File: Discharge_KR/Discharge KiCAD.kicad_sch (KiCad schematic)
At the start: 13 parts, among them IC1 AL5890-10D-13, J105 Conn_01x02, J3 Conn_01x02, J4 Conn_01x03, J90 Conn_01x02, K1 DBR71210, Q1 2N7000, U2 HCPL-817-000E

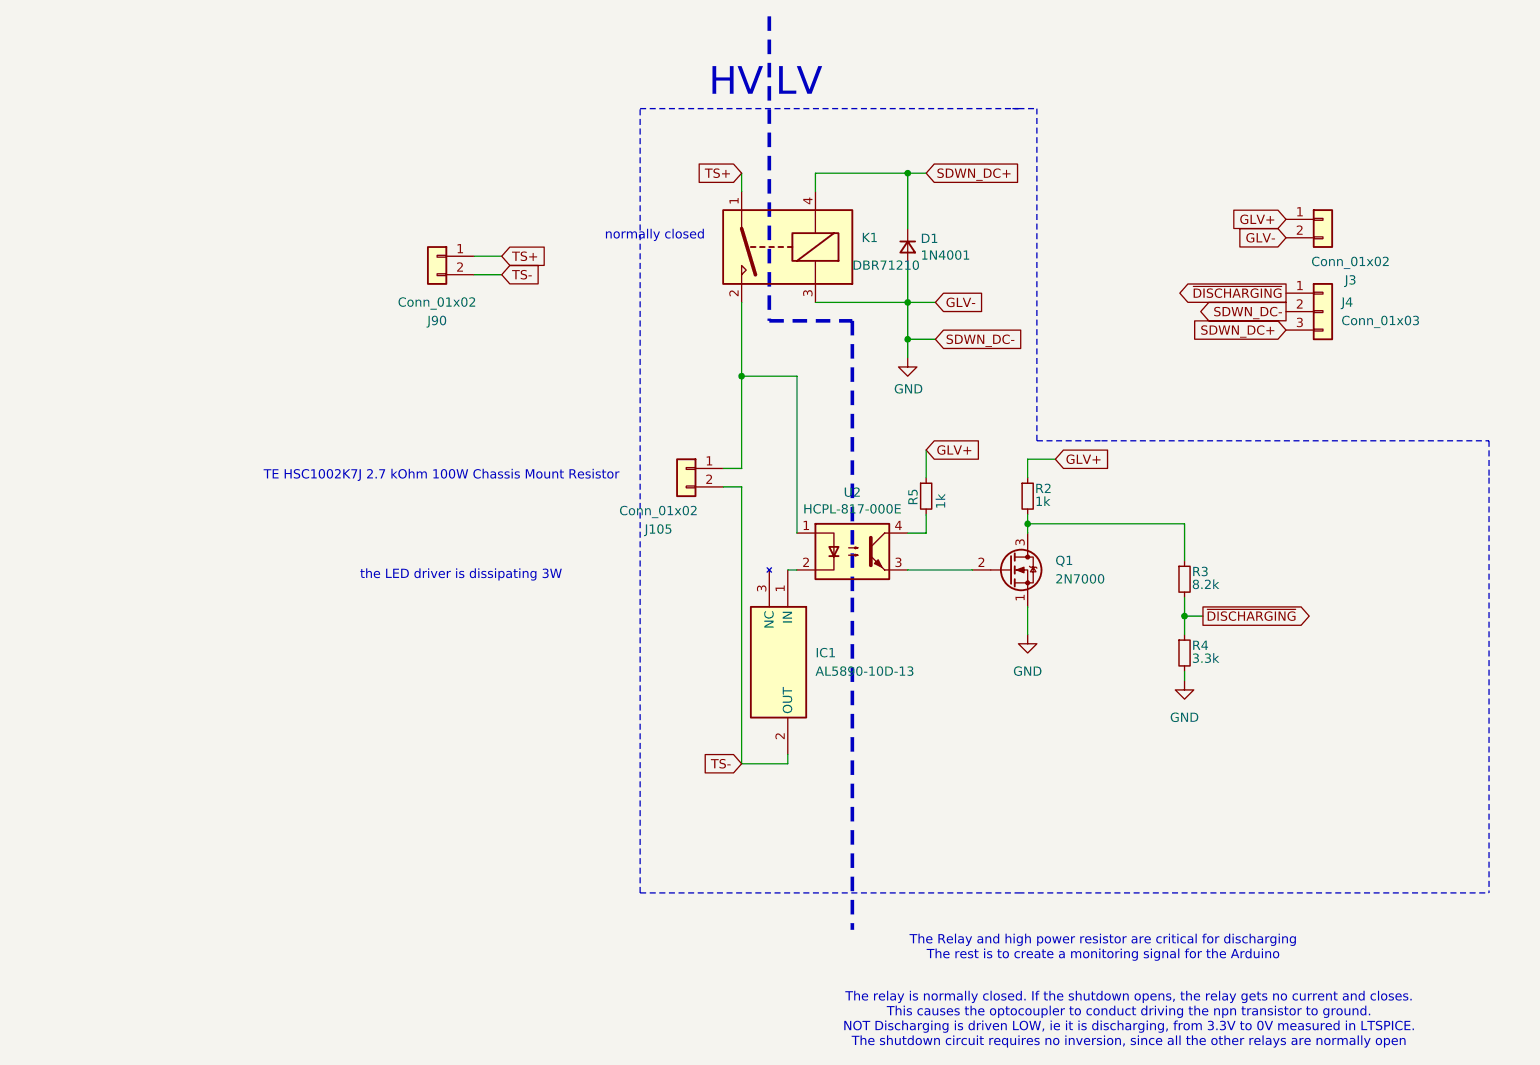
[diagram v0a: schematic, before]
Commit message: precharge and discharge fixed
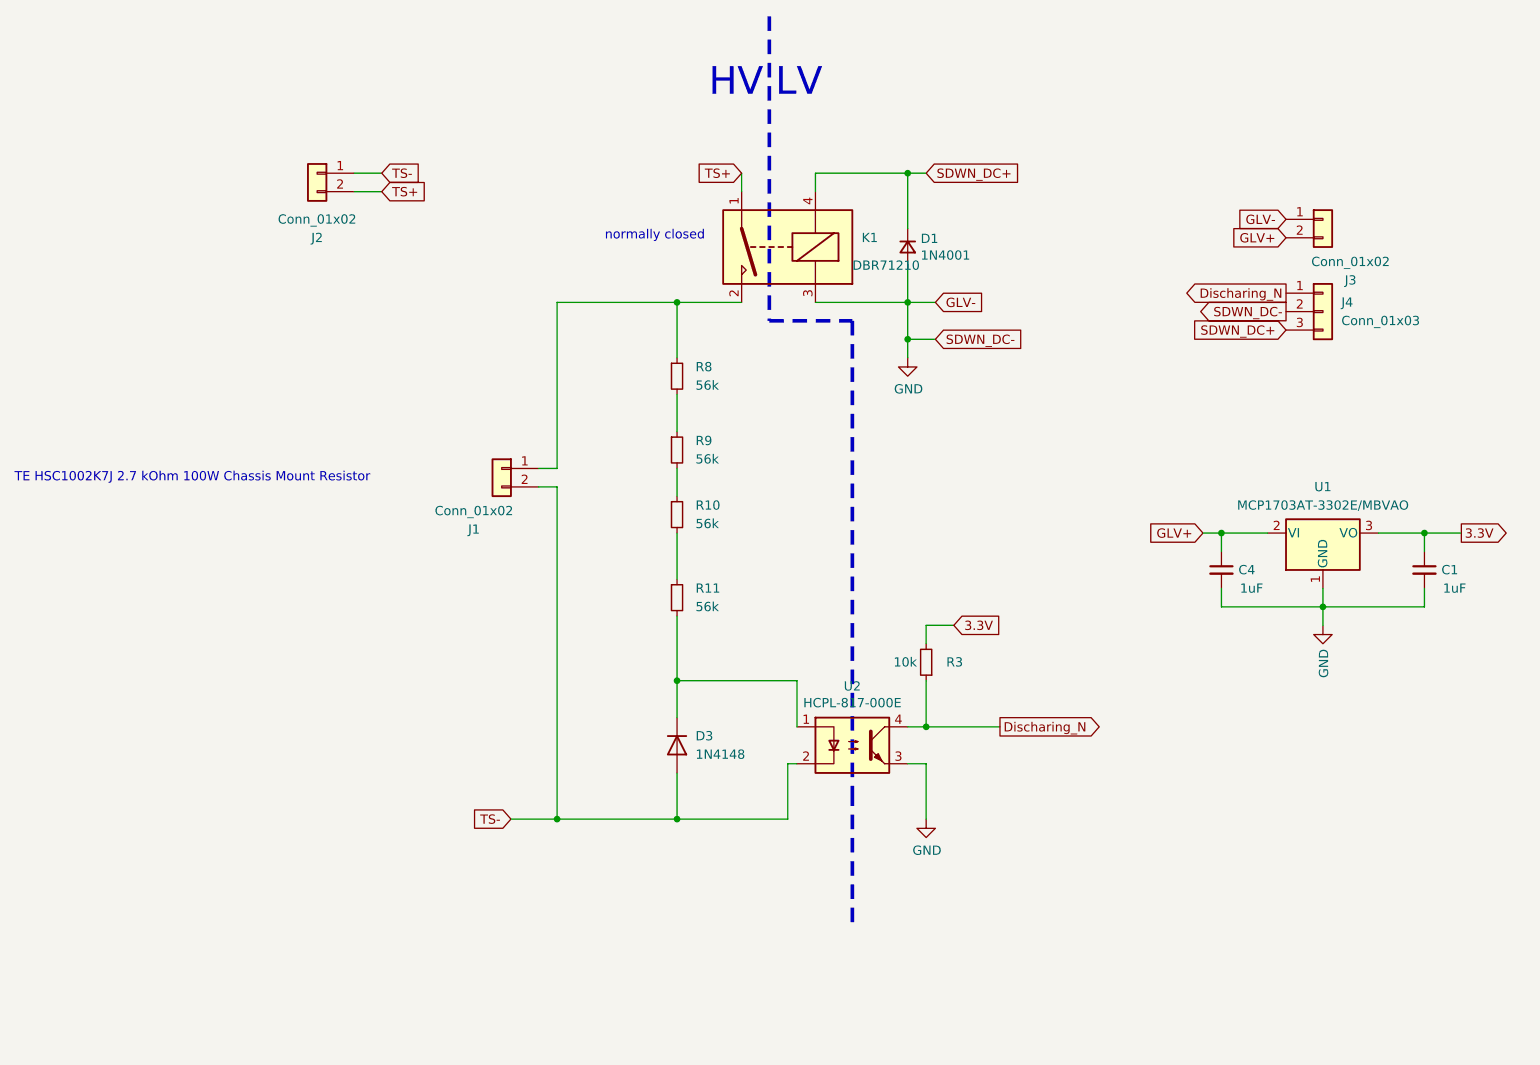
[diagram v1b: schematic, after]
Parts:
- removed IC1: AL5890-10D-13, AL5890_10_D13:AL589010D13, symbol AL5890-10D-13:AL5890-10D-13
- removed Q1: 2N7000, Package_TO_SOT_THT:TO-92_Inline, symbol Transistor_FET:2N7000
- removed R2, R5: 1k, Resistor_THT:R_Axial_DIN0207_L6.3mm_D2.5mm_P10.16mm_Horizontal, symbol Device:R_Small
- removed R4: 3.3k, Resistor_THT:R_Axial_DIN0207_L6.3mm_D2.5mm_P10.16mm_Horizontal, symbol Device:R_Small
- added C1, C4: 1uF, FA14_Capacitor:FA18X7R1H104KNU00, symbol tsal-rescue:C_Small-Device
- added D3: 1N4148, Diode_THT:D_DO-35_SOD27_P7.62mm_Horizontal, symbol Diode:1N4148
- added R10, R11, R8, R9: 56k, Resistor_THT:R_Axial_DIN0207_L6.3mm_D2.5mm_P10.16mm_Horizontal, symbol Device:R_Small
- added U1: MCP1703AT-3302E/MBVAO, Package_TO_SOT_SMD:SOT-89-3, symbol Regulator_Linear:MCP1703Ax-300xxMB
- J3: footprint Phoenix 1x2 Connector:Phoenix_1x2_1729128 -> Connector_JST:JST_XH_B2B-XH-A_1x02_P2.50mm_Vertical; Part Number 1729128 -> B2B-XH-A
- R3: value 8.2k -> 10k; Part Number MCF 0.25W 8K2 -> MCF 0.25W 10K
- renumbered J105 to J1, J90 to J2
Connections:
- net GLV+: now also J3.2 (Pin_2), C4.1, U1.2 (VI); no longer J3.1 (Pin_1)
- net GND: now also J3.1 (Pin_1), U2.3, C1.2, C4.2, U1.1 (GND); no longer J3.2 (Pin_2)
- net TS+: now also J2.2 (Pin_2); no longer J2.1 (Pin_1)
- net TS-: now also J2.1 (Pin_1), U2.2, D3.2 (A); no longer J2.2 (Pin_2)
- net at J1.1 (Pin_1), K1.2: now also R8.1; no longer U2.1
- net Discharing_N: now reaches U2.4
- net Discharing_N: now also J4.1 (Pin_1), R3.1
- net ~{DISCHARGING} renamed 3.3V
- net 3.3V: now also C1.1, U1.3 (VO); no longer J4.1 (Pin_1)
- new net: R8.2, R9.1
- new net: R10.1, R9.2
- new net: D3.1 (K), R11.2, U2.1
- new net: R10.2, R11.1
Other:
- note removed: "The Relay and high power resistor are critical for discharging The rest is to create a monitoring signal for the Arduino"
- note removed: "The relay is normally closed. If the shutdown opens, the relay gets no current and closes. This causes the optocoupler to conduct driving the npn transistor to ground. NOT Discharging is driven LOW, ie it is discharging, from 3.3V to 0V measured in LTSPICE. The shutdown circuit requires no inversion, since all the other relays are normally open"
- note removed: "the LED driver is dissipating 3W"
- moved on the sheet: J1, J2, U2

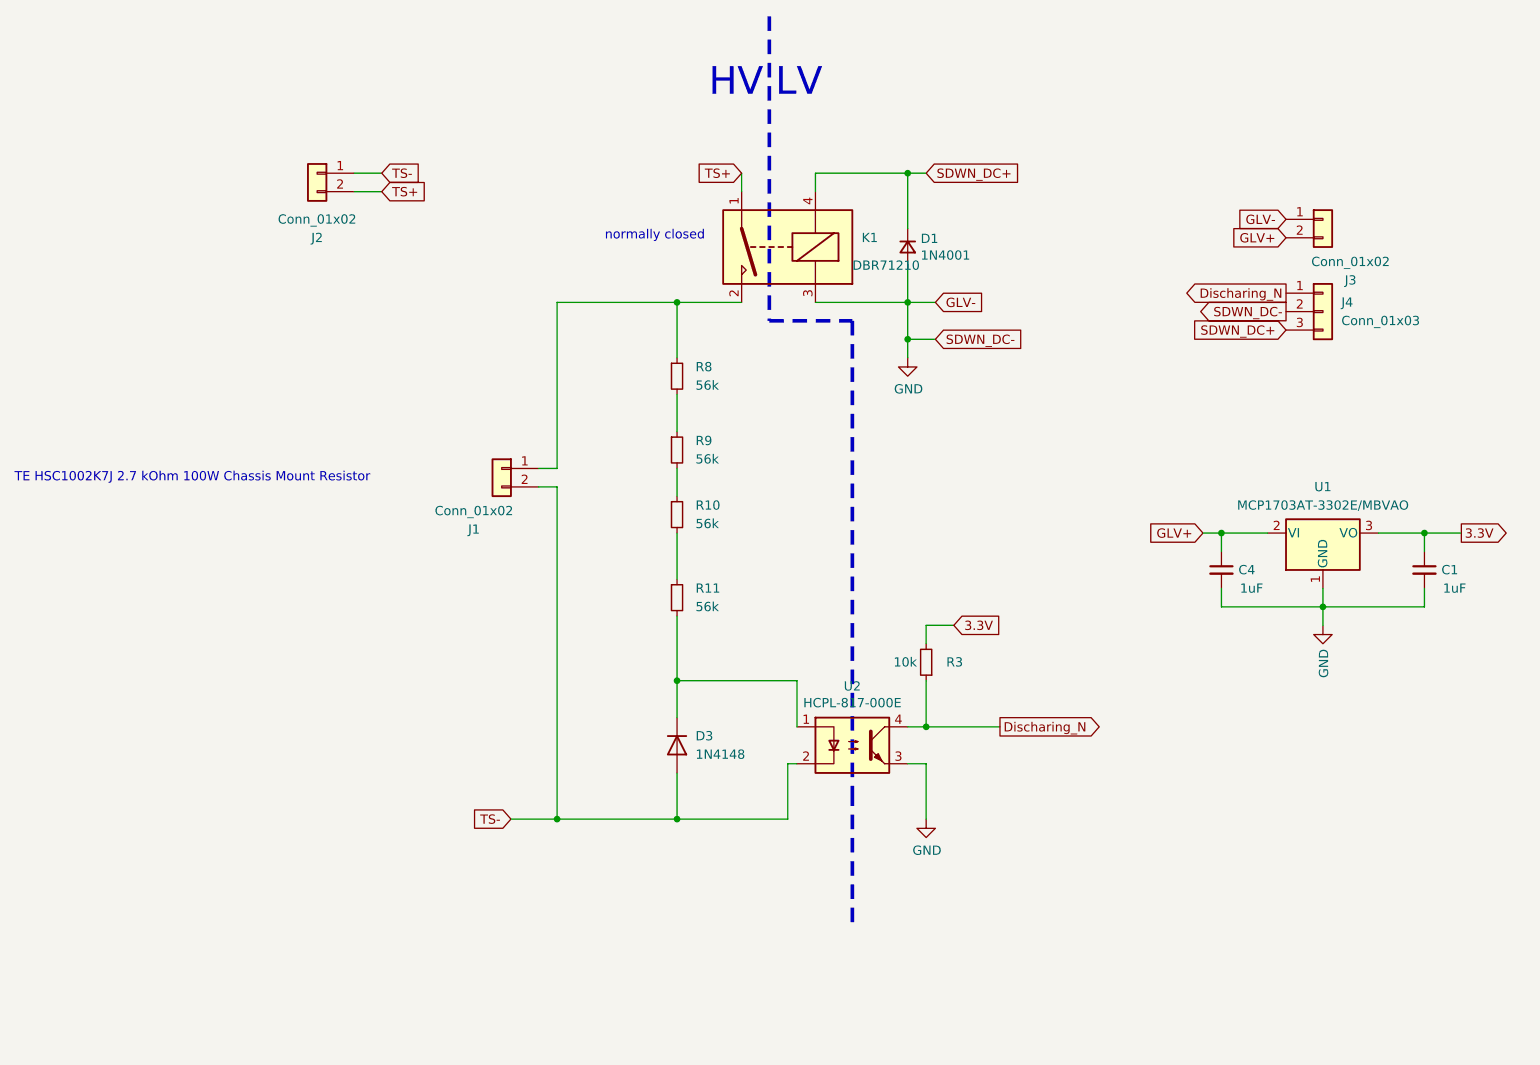
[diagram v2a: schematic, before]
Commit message: Slave with SMD and no other fuses
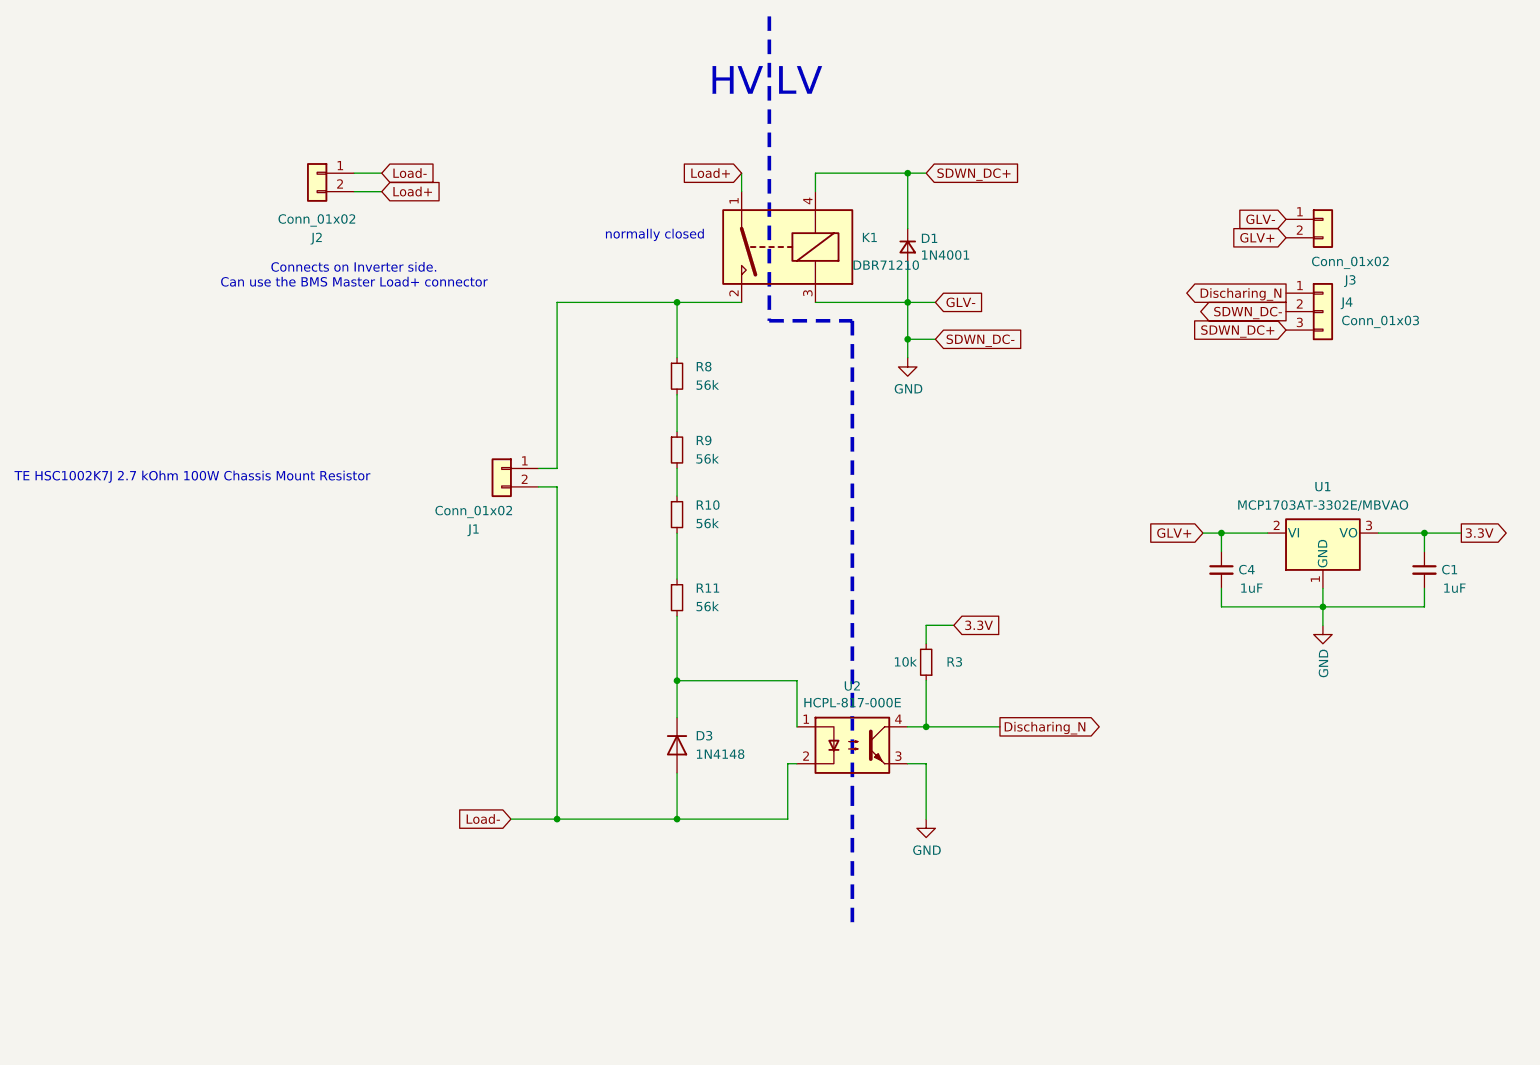
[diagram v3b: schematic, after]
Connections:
- net TS+ renamed Load+
- net TS- renamed Load-
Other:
- note added: "Connects on Inverter side. Can use the BMS Master Load+ connector"
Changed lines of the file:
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@@
+		)
+	)
+	(text "Connects on Inverter side.\nCan use the BMS Master Load+ connector"
+		(exclude_from_sim no)
+		(at 40.64 45.974 0)
+		(effects
+			(font
+				(size 1.27 1.27)
+			)
 		)
 	)
@@
 		)
 	)
-	(global_label "TS+"
+	(global_label "Load+"
 		(shape input)
 		(at 44.45 34.29 0)
@@
 		)
 		(property "Intersheetrefs" "${INTERSHEET_REFS}"
-			(at 50.5305 34.29 0)
+			(at 52.8285 34.29 0)
 			(effects
 				(font
@@
 		)
 	)
-	(global_label "TS-"
+	(global_label "Load-"
 		(shape input)
 		(at 62.23 120.65 180)
@@
 		)
 		(property "Intersheetrefs" "${INTERSHEET_REFS}"
-			(at 56.1495 120.65 0)
+			(at 53.8515 120.65 0)
 			(effects
 				(font
@@
 		)
 	)
-	(global_label "TS-"
+	(global_label "Load-"
 		(shape input)
 		(at 44.45 31.75 0)
@@
 		)
 		(property "Intersheetrefs" "${INTERSHEET_REFS}"
-			(at 50.5305 31.75 0)
+			(at 52.8285 31.75 0)
 			(effects
 				(font
@@
 		)
 	)
-	(global_label "TS+"
+	(global_label "Load+"
 		(shape input)
 		(at 93.98 31.75 180)
@@
 		)
 		(property "Intersheetrefs" "${INTERSHEET_REFS}"
-			(at 87.8995 31.75 0)
-			(effects
-				(font
+			(at 85.6015 31.75 0)
+			(effects
+				(font
